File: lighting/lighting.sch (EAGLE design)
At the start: 6 parts, among them J1 22-05-3021

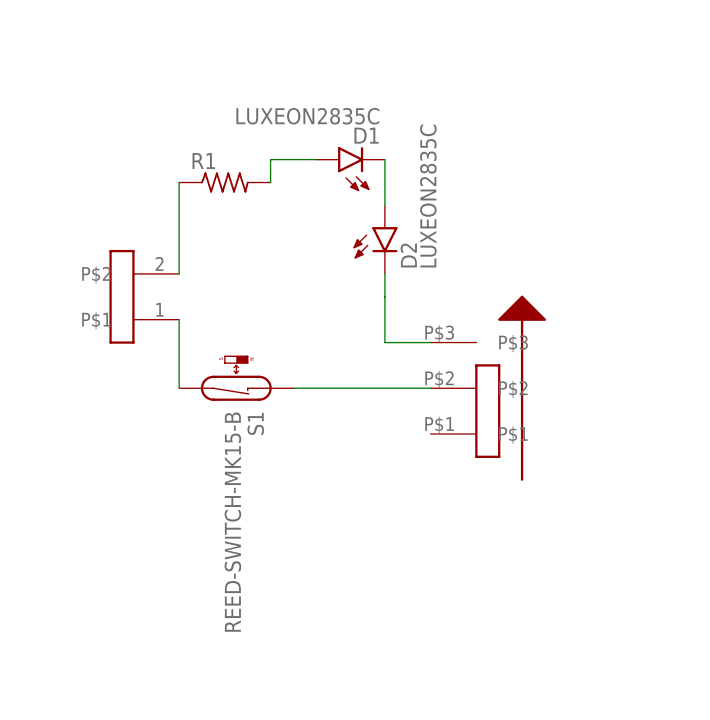
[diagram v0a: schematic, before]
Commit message: fixed LED direction; GND plane
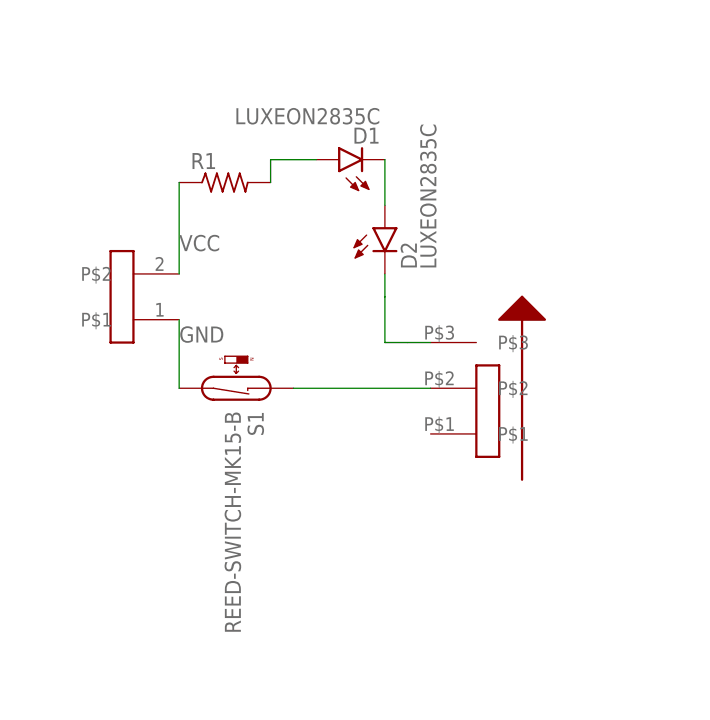
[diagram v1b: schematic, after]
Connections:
- net N$1 renamed GND
- net N$6 renamed VCC
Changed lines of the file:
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@@
 <grid distance="0.1" unitdist="inch" unit="inch" style="lines" multiple="1" display="no" altdistance="0.01" altunitdist="inch" altunit="inch"/>
 <layers>
-<layer number="1" name="Top" color="4" fill="1" visible="yes" active="no"/>
-<layer number="16" name="Bottom" color="1" fill="1" visible="yes" active="no"/>
-<layer number="17" name="Pads" color="2" fill="1" visible="yes" active="no"/>
-<layer number="18" name="Vias" color="2" fill="1" visible="yes" active="no"/>
-<layer number="19" name="Unrouted" color="6" fill="1" visible="yes" active="no"/>
-<layer number="20" name="Dimension" color="24" fill="1" visible="yes" active="no"/>
-<layer number="21" name="tPlace" color="7" fill="1" visible="yes" active="no"/>
-<layer number="22" name="bPlace" color="7" fill="1" visible="yes" active="no"/>
-<layer number="23" name="tOrigins" color="15" fill="1" visible="yes" active="no"/>
-<layer number="24" name="bOrigins" color="15" fill="1" visible="yes" active="no"/>
-<layer number="25" name="tNames" color="7" fill="1" visible="yes" active="no"/>
-<layer number="26" name="bNames" color="7" fill="1" visible="yes" active="no"/>
-<layer number="27" name="tValues" color="7" fill="1" visible="yes" active="no"/>
-<layer number="28" name="bValues" color="7" fill="1" visible="yes" active="no"/>
+<layer number="1" name="Top" color="4" fill="1" visible="no" active="no"/>
+<layer number="16" name="Bottom" color="1" fill="1" visible="no" active="no"/>
+<layer number="17" name="Pads" color="2" fill="1" visible="no" active="no"/>
+<layer number="18" name="Vias" color="2" fill="1" visible="no" active="no"/>
+<layer number="19" name="Unrouted" color="6" fill="1" visible="no" active="no"/>
+<layer number="20" name="Dimension" color="24" fill="1" visible="no" active="no"/>
+<layer number="21" name="tPlace" color="7" fill="1" visible="no" active="no"/>
+<layer number="22" name="bPlace" color="7" fill="1" visible="no" active="no"/>
+<layer number="23" name="tOrigins" color="15" fill="1" visible="no" active="no"/>
+<layer number="24" name="bOrigins" color="15" fill="1" visible="no" active="no"/>
+<layer number="25" name="tNames" color="7" fill="1" visible="no" active="no"/>
+<layer number="26" name="bNames" color="7" fill="1" visible="no" active="no"/>
+<layer number="27" name="tValues" color="7" fill="1" visible="no" active="no"/>
+<layer number="28" name="bValues" color="7" fill="1" visible="no" active="no"/>
 <layer number="29" name="tStop" color="7" fill="3" visible="no" active="no"/>
 <layer number="30" name="bStop" color="7" fill="6" visible="no" active="no"/>
@@
 <layer number="35" name="tGlue" color="7" fill="4" visible="no" active="no"/>
 <layer number="36" name="bGlue" color="7" fill="5" visible="no" active="no"/>
-<layer number="37" name="tTest" color="7" fill="1" visible="yes" active="no"/>
-<layer number="38" name="bTest" color="7" fill="1" visible="yes" active="no"/>
+<layer number="37" name="tTest" color="7" fill="1" visible="no" active="no"/>
+<layer number="38" name="bTest" color="7" fill="1" visible="no" active="no"/>
 <layer number="39" name="tKeepout" color="4" fill="11" visible="no" active="no"/>
 <layer number="40" name="bKeepout" color="1" fill="11" visible="no" active="no"/>
@@
 <layer number="44" name="Drills" color="7" fill="1" visible="no" active="no"/>
 <layer number="45" name="Holes" color="7" fill="1" visible="no" active="no"/>
-<layer number="46" name="Milling" color="3" fill="1" visible="yes" active="no"/>
-<layer number="47" name="Measures" color="7" fill="1" visible="yes" active="no"/>
-<layer number="48" name="Document" color="7" fill="1" visible="yes" active="no"/>
-<layer number="49" name="Reference" color="7" fill="1" visible="yes" active="no"/>
-<layer number="51" name="tDocu" color="7" fill="1" visible="yes" active="no"/>
-<layer number="52" name="bDocu" color="7" fill="1" visible="yes" active="no"/>
+<layer number="46" name="Milling" color="3" fill="1" visible="no" active="no"/>
+<layer number="47" name="Measures" color="7" fill="1" visible="no" active="no"/>
+<layer number="48" name="Document" color="7" fill="1" visible="no" active="no"/>
+<layer number="49" name="Reference" color="7" fill="1" visible="no" active="no"/>
+<layer number="51" name="tDocu" color="7" fill="1" visible="no" active="no"/>
+<layer number="52" name="bDocu" color="7" fill="1" visible="no" active="no"/>
 <layer number="88" name="SimResults" color="9" fill="1" visible="yes" active="yes"/>
 <layer number="89" name="SimProbes" color="9" fill="1" visible="yes" active="yes"/>
@@
 </busses>
 <nets>
-<net name="N$1" class="0">
+<net name="GND" class="0">
 <segment>
 <pinref part="S1" gate="G$1" pin="2"/>
 <wire x1="40.64" y1="58.42" x2="40.64" y2="50.8" width="0.1524" layer="91"/>
 <pinref part="J1" gate="G$1" pin="P$1"/>
+<label x="40.64" y="55.88" size="1.778" layer="95"/>
 </segment>
 </net>
@@
 </segment>
 </net>
-<net name="N$6" class="0">
+<net name="VCC" class="0">
 <segment>
 <pinref part="R1" gate="G$1" pin="1"/>
 <wire x1="40.64" y1="73.66" x2="40.64" y2="63.5" width="0.1524" layer="91"/>
 <pinref part="J1" gate="G$1" pin="P$2"/>
+<label x="40.64" y="66.04" size="1.778" layer="95"/>
 </segment>
 </net>

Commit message: added sim; added switch-off timer; updated pcb
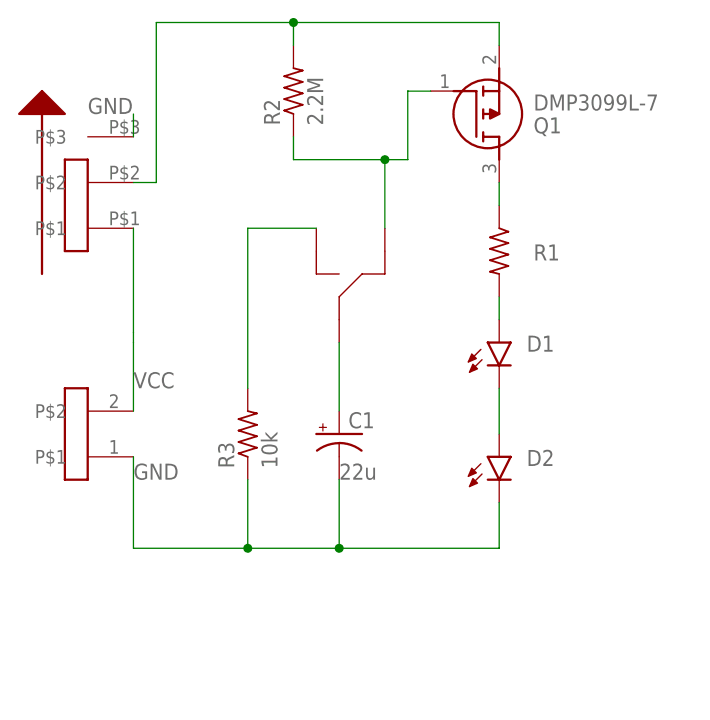
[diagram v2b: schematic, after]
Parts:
- removed S1: REED-SWITCH-MK15-B, switch-reed:REED-SWITCH-MK15-B
- added C1: WE-CAP, my_lib:WE-CAP
- added Q1: DMP3099L-7, SamacSys_Parts:DMP3099L-7
- added R2: 2.2M, rcl:R-US_R1206
- added R3: 10k, rcl:R-US_R1206
- added U$1: KSK-1C90U, my_lib:KSK-1C90U
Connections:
- removed net N$2 (its old number): S1.1, S2.P$2
- new net COM: C1.+, U$1.COM
- new net NC: Q1.G, R2.1, U$1.NC
- new net NO: R3.2, U$1.NO
- new net PWR: Q1.S, R2.2, S2.P$2
- net GND: now also C1.-, D2.C, R3.1, S2.P$3; no longer S1.2
- net N$3: now also Q1.D, R1.1; no longer D2.C, S2.P$3
- net VCC: now also S2.P$1; no longer R1.1
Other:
- moved on the sheet: D1, D2, R1
